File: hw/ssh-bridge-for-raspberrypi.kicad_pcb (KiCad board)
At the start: 2 copper layers, 93 x 50 mm, 38 parts, among them J101 USB4105-GF-A, J102 USB4105-GF-A, J103 PinHeader Conn_01x08, J104 Conn_02x05_Odd_Even, J105 USB_A, J106 Conn_01x03, SW304 1, U101 ST7789V_TFT_DISPLAY, U102 TLP3555A, U103 AZ1117-CH3.3TRG1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

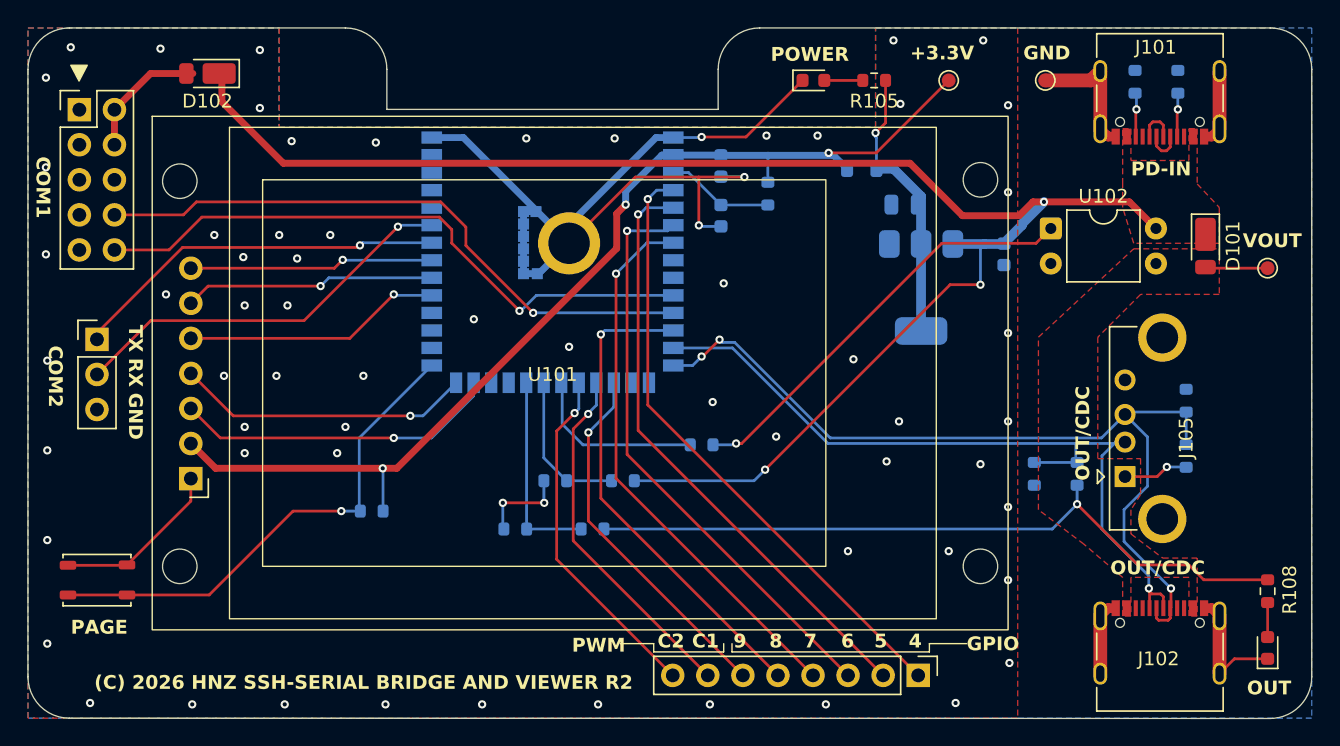
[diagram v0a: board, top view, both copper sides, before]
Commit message: Update ST7789V new 8pin foot print
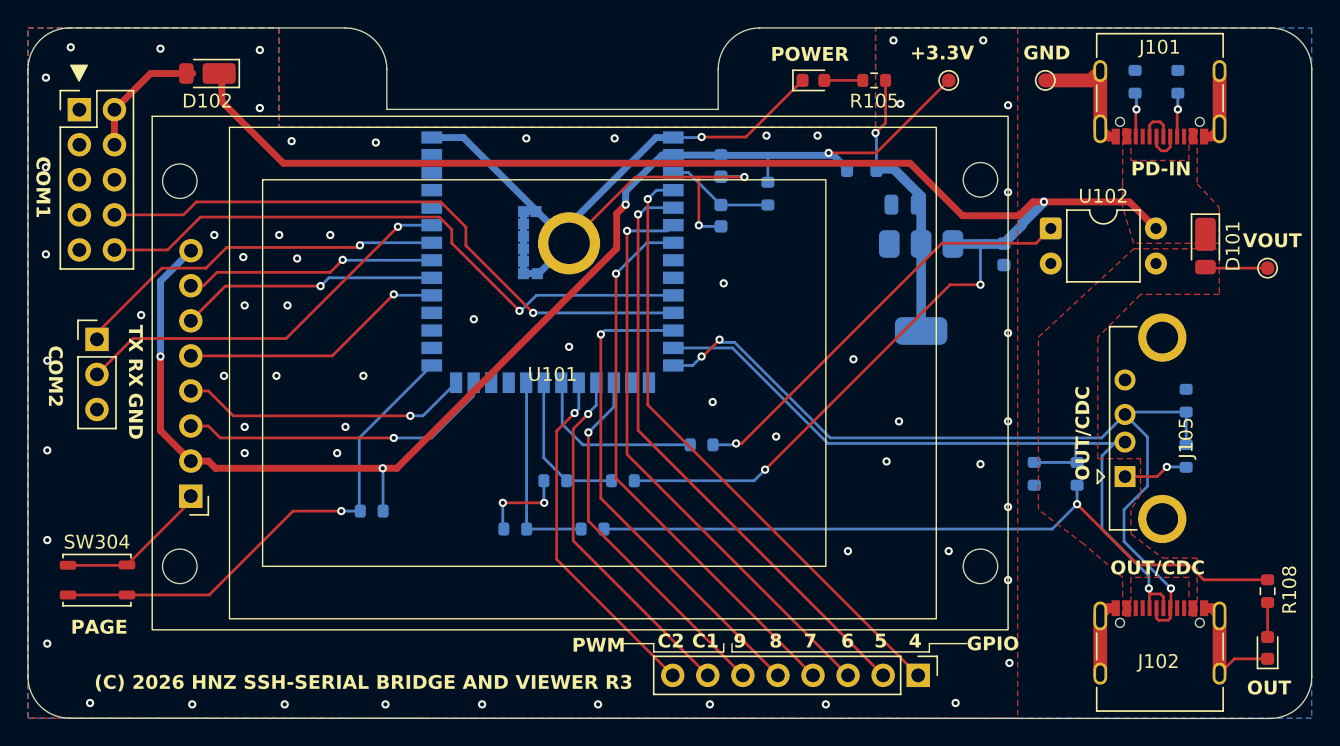
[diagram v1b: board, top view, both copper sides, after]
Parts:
- J101, J102: footprint tbctl:USB_C_5077CR-16-SMC2-BK-TR -> Library:USB_C_5077CR-16-SMC2-BK-TR
- J105: footprint tbctl:USB_A_5075AR-04 -> Library:USB_A_5075AR-04
- SW304: footprint tbctl:SW_SKRPACE010_4mm_3mm -> Library:SW_SKRPACE010_4mm_3mm
- U101: value ST7789V_TFT_DISPLAY -> ST7789V_TFT_DISPLAY_8P; footprint tbctl:ST7789V TFT SPI DISPLAY 320x240 -> Library:ST7789V TFT SPI DISPLAY 320x240 GMT020-02-8P
- U201: footprint tbctl:ESP32-S3-WROOM-1_EXP -> Library:ESP32-S3-WROOM-1_EXP
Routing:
- net +3.3V: track 76.1 -> 92.6 mm, vias 3 -> 4
- net GND: track 118.4 -> 116.7 mm
- net /IO39: track 18.2 -> 18.7 mm
- net /IO48: track 23.6 -> 23.1 mm
- net /IO40: track 17.7 -> 18.2 mm
- net /IO38: track 18.8 -> 19.3 mm
- net /IO45: track 21.5 -> 21.0 mm
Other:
- board text added: "(C) 2026 HNZ SSH-SERIAL BRIDGE AND VIEWER R3"
- board text removed: "(C) 2026 HNZ SSH-SERIAL BRIDGE AND VIEWER R2"
